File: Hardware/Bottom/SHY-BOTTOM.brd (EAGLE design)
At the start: 33 x 33 mm, 32 parts, among them U1 AD5242-SO16

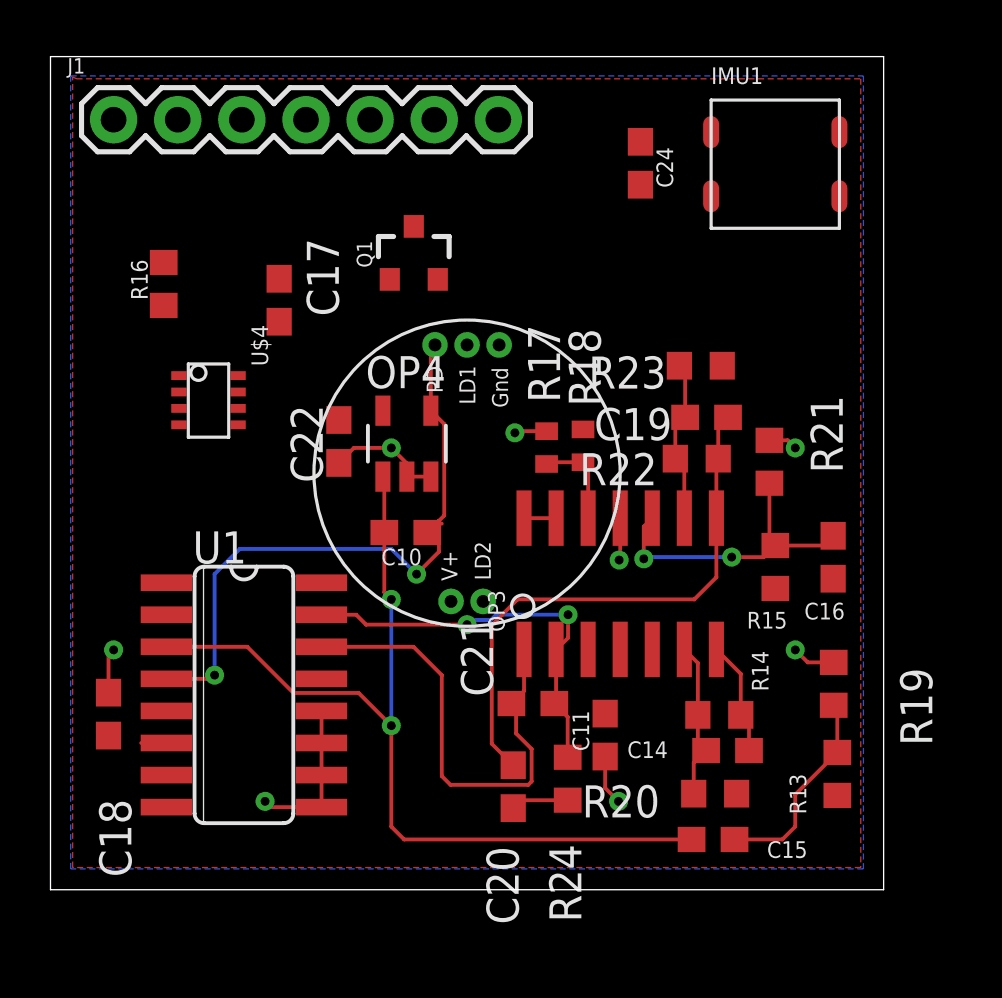
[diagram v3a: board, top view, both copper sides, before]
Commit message: finish bottom board
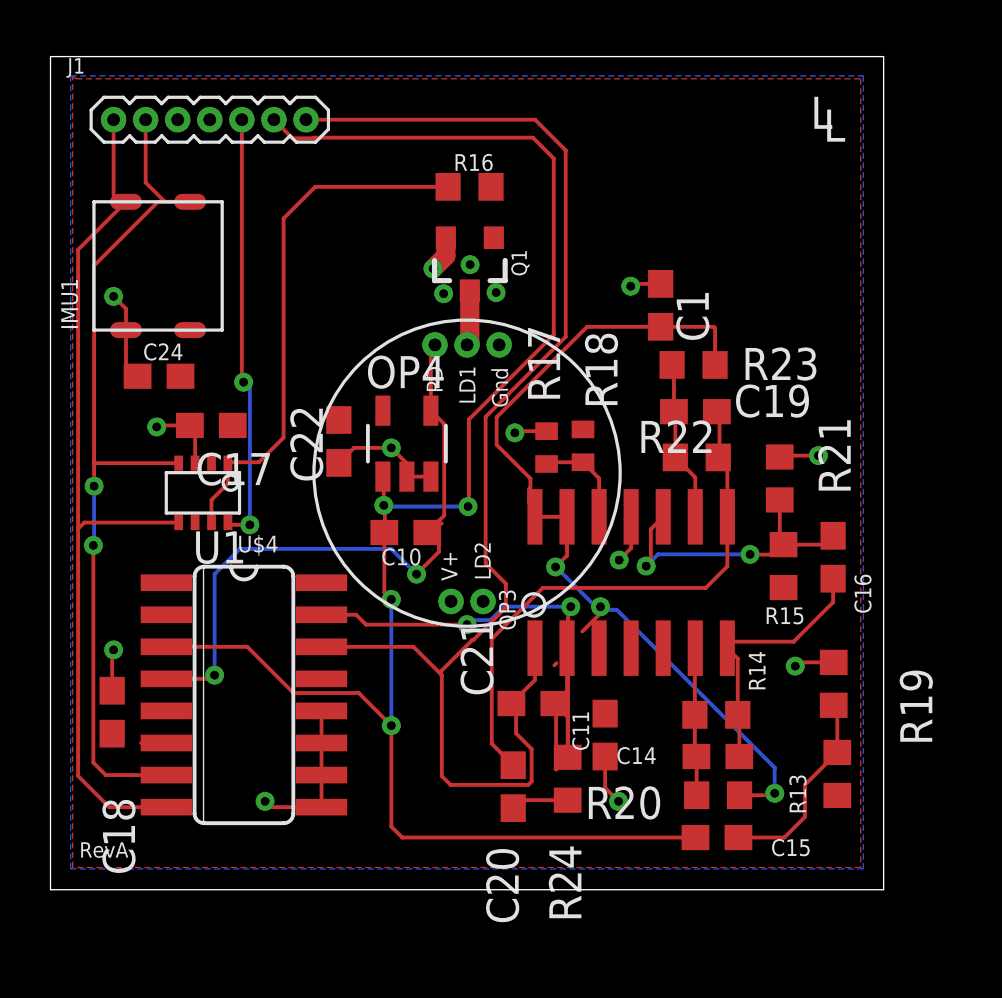
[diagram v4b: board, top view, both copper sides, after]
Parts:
- added C1: 100n, LinnesLab-Passives:C0603
- added LOGO1: REVISION.A, LinnesLab-Logos:REV.A
- added LOGO2: LINNES.LAB.LOGO, LinnesLab-Logos:LINNES.LAB.LOGO
- J1: device LinnesLab-Connectors:1X07 -> LinnesLab-Connectors:1X07_1.27MM
- moved IMU1 24.8 mm to (6.76, 27.2), turned to 90 degrees
- moved C24 20.9 mm to (6.80, 22.8), turned to 0 degrees
- moved R16 12.7 mm to (19.1, 30.3), turned to 0 degrees
- moved C17 5.64 mm to (8.87, 20.9), turned to 0 degrees
- moved U$4 3.66 mm to (8.54, 18.2), turned to 180 degrees
- moved Q1 2.25 mm to (19.1, 27.3), turned to 180 degrees
- moved R21 0.78 mm to (31.4, 18.8)
- moved C19 0.50 mm to (28.0, 21.4)
- moved C14 0.45 mm to (28.9, 7.78)
- moved OP3 0.44 mm to (25.5, 14.7)
- moved R15 0.33 mm to (31.5, 15.3)
- moved R23 0.29 mm to (28.0, 23.3)
- moved C15 0.17 mm to (28.9, 4.57)
- moved C18 0.16 mm to (4.94, 9.53)
- moved R20 0.13 mm to (28.9, 6.24)
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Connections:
- removed net N$2: J1.4
- removed net N$3: J1.3
- removed net N$4: J1.2
- removed net N$5: J1.1
- net 3.3V: now also J1.4
- net A6/TIA: now also J1.6; no longer J1.5
- net D29/LED.CTRL: now also J1.5; no longer J1.6
- net GND: now also C1.1, J1.3
- net SCL: now also J1.2
- net SDA: now also J1.1
- net VREF: now also C1.2
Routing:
- net SCL: track 0.00 -> 35.6 mm, vias 0 -> 2
- net VREF: track 1.27 -> 36.5 mm, vias 0 -> 3
- net SDA: track 0.00 -> 34.6 mm
- net A7/PPG: track 19.5 -> 54.0 mm
- net A6/TIA: track 36.3 -> 66.7 mm, vias 2 -> 4
- net N$9: track 0.00 -> 21.0 mm
- net D29/LED.CTRL: track 0.00 -> 17.1 mm, vias 0 -> 2
- net GND: track 20.5 -> 30.0 mm, vias 8 -> 12
- net G.W2: track 16.7 -> 25.2 mm
- net N$16: track 4.54 -> 10.4 mm
- net LED.C: track 0.00 -> 2.19 mm
